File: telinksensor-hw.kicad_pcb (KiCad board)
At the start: 2 copper layers, 69 parts, among them Q1 2N7002, U1 TLSR8258

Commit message: Outline done
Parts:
- added AE1: Antenna, RF_Antenna:Johanson_2450AT18x100, F.Cu at (156.0, 46.4)
- added H1: MountingHole, MountingHole:MountingHole_3.2mm_M3_Pad_Via, F.Cu at (149.5, 104.4)
- added H2: MountingHole, MountingHole:MountingHole_3.2mm_M3_Pad_Via, F.Cu at (182.3, 104.5)
- added J1: ANT, Connector_Coaxial:U.FL_Molex_MCRF_73412-0110_Vertical, F.Cu at (150.1, 47.7)
- added J2: 3W RTD, TerminalBlock:TerminalBlock_bornier-3_P5.08mm, F.Cu at (176.1, 112.8)
- added J4: RTD 2W, TerminalBlock:TerminalBlock_bornier-2_P5.08mm, F.Cu at (160.8, 112.8)
- added J5: SOIC bite, soicbite:SOIC_clipProgSmall, F.Cu at (185.2, 73.4)
- added L1: 47u, Inductor_SMD:L_0805_2012Metric, F.Cu at (120.4, 46.5)
- added L2: 1n3, Inductor_SMD:L_0402_1005Metric, F.Cu at (126.5, 109.7)
- added L3: 3n3, Inductor_SMD:L_0402_1005Metric, F.Cu at (114.5, 73.8)
- added SW1: SW_Push, Button_Switch_SMD:SW_SPST_EVQPE1, F.Cu at (180.9, 112.9)
- added U2: SHT40, sensirion:SHT40, F.Cu at (186.2, 115.6)
- added U3: BMP390, bosh:BMP390, F.Cu at (145.7, 115.3)
- added Y1: 24MHz, Crystal:Crystal_SMD_3225-4Pin_3.2x2.5mm, F.Cu at (109.9, 74.8)
- C19, C20, C21, C22, C23, C24: footprint Capacitor_SMD:C_0603_1608Metric -> Capacitor_SMD:C_0402_1005Metric
- R8: footprint Resistor_SMD:R_0603_1608Metric -> Resistor_SMD:R_0402_1005Metric
- TP1, TP10, TP2, TP3, TP4, TP5, TP6, TP7, TP8, TP9: footprint TestPoint:TestPoint_Pad_1.5x1.5mm -> TestPoint:TestPoint_Pad_D1.0mm
- moved R2 63.8 mm to (166.5, 131.2)
- moved R8 60.6 mm to (150.1, 51.8), turned to 90 degrees
- moved R14 58.8 mm to (85.2, 42.7)
- moved R18 58.8 mm to (57.0, 58.9)
- moved R19 58.8 mm to (57.0, 63.9)
- moved R9 58.8 mm to (85.2, 45.2)
- moved TP1 58.8 mm to (80.3, 61.9)
- moved TP5 58.8 mm to (90.1, 53.3)
- moved C11 58.8 mm to (70.8, 52.8)
- moved C12 58.8 mm to (65.0, 64.8)
- moved C16 58.8 mm to (73.0, 57.8)
- moved C18 58.8 mm to (70.8, 50.3)
- moved C19 58.8 mm to (82.8, 50.3)
- moved C2 58.8 mm to (73.1, 45.2)
- moved C20 58.8 mm to (73.0, 60.3)
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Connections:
- R8 pad 1: Net-(AE1-Pad1) -> Net-(C20-Pad1)
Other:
- board outline added: 44 x 33.5 mm
- copper layers 2 -> 4

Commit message: Routing mostly done
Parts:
- removed C24: 1p, Capacitor_SMD:C_0402_1005Metric
- removed C29: 100n, Capacitor_SMD:C_0603_1608Metric
- AE1: value Antenna -> Antenna_Shield; footprint RF_Antenna:Johanson_2450AT18x100 -> RF_Antenna:Texas_SWRA117D_2.4GHz_Left
- C10, C12, C13, C14, C15, C16, C28, C3, C30, C5, C6, C7, C8, C9: footprint Capacitor_SMD:C_0603_1608Metric -> Capacitor_SMD:C_0402_1005Metric
- C17: value 100n -> 1p; footprint Capacitor_SMD:C_0603_1608Metric -> Capacitor_SMD:C_0402_1005Metric
- C18: value 1u -> 100p; footprint Capacitor_SMD:C_0603_1608Metric -> Capacitor_SMD:C_0402_1005Metric
- C20: value 2p7 -> 0p5
- C21: value 220p -> 2p7
- C22: value 2p -> 220p
- C23: value 0p5 -> 2p
- moved C30 139.2 mm to (186.2, 113.3), turned to 180 degrees
- moved D3 121.4 mm to (171.1, 102.1), turned to 180 degrees
- moved D2 121.0 mm to (167.1, 102.1)
- moved R5 118.9 mm to (176.9, 100.7), turned to 180 degrees
- moved C26 118.1 mm to (169.1, 106.4)
- moved TP4 115.6 mm to (185.9, 99.1), turned to 180 degrees
- moved C11 115.2 mm to (176.9, 97.7), turned to 180 degrees
- moved Q1 115.2 mm to (163.1, 106.7), turned to -90 degrees
- moved R17 114.3 mm to (174.3, 103.9), turned to 90 degrees
- moved C18 113.2 mm to (176.2, 91.5), turned to 90 degrees
- moved C25 112.9 mm to (167.5, 104.7)
- moved R18 112.9 mm to (159.4, 106.3)
- moved R19 111.5 mm to (159.4, 107.9)
- moved D4 111.1 mm to (156.0, 106.7), turned to 90 degrees
- moved U1 111.0 mm to (157.0, 96.5), turned to -90 degrees
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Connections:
- AE1 pad 2: (no net) -> GND
- C17 pad 1: VDD -> Net-(AE1-Pad1)
- C18 pad 1: VDD -> Net-(L3-Pad2)
- C18 pad 2: GND -> Net-(AE1-Pad1)
- C20 pad 1: Net-(C20-Pad1) -> Net-(L3-Pad2)
- C21 pad 1: Net-(C20-Pad1) -> Net-(C21-Pad1)
- C21 pad 2: Net-(C21-Pad2) -> GND
- C22 pad 1: Net-(C21-Pad2) -> Net-(C21-Pad1)
- C22 pad 2: GND -> Net-(C22-Pad2)
- C23 pad 1: Net-(AE1-Pad1) -> Net-(C22-Pad2)
- L2 pad 2: Net-(C20-Pad1) -> Net-(C21-Pad1)
- L3 pad 1: Net-(C21-Pad2) -> Net-(C22-Pad2)
- L3 pad 2: Net-(AE1-Pad1) -> Net-(L3-Pad2)
- R8 pad 1: Net-(C20-Pad1) -> Net-(L3-Pad2)
- U1 pad 27: Net-(C20-Pad1) -> Net-(C21-Pad1)
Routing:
- net /GND_RTD: track 0.00 -> 29.8 mm
- net /PGA-: track 0.00 -> 21.3 mm
- net /SENSOR_PWR: track 0.00 -> 21.2 mm
- net /PGA+: track 0.00 -> 21.1 mm
- net /I2C_SDA: track 0.00 -> 18.5 mm, vias 0 -> 2
- net Net-(C1-Pad1): track 0.00 -> 16.5 mm
- net /I2C_SCL: track 0.00 -> 16.5 mm, vias 0 -> 2
- net VDD: track 0.00 -> 16.3 mm, vias 0 -> 4
- net GND: track 0.00 -> 16.2 mm, vias 0 -> 88
- net /ADC3: track 0.00 -> 16.1 mm
- net Net-(J2-Pad3): track 0.00 -> 15.8 mm, vias 0 -> 1
- net +1V2: track 0.00 -> 15.8 mm, vias 0 -> 6
- net Net-(R13-Pad2): track 0.00 -> 14.9 mm
- net /SWM: track 0.00 -> 14.4 mm, vias 0 -> 1
- net Net-(L3-Pad2): track 0.00 -> 11.7 mm
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- added copper zone on B.Cu, net GND
- added copper zone on F.Cu, net GND
- added copper zone on In1.Cu, net GND
- added copper zone on In2.Cu, net VDD

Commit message: Routing almost done
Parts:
- D1, J2, J4, SW1: moved to B.Cu
- moved J2 10.2 mm to (165.9, 112.8), turned to 0 degrees
- moved J4 5.08 mm to (155.8, 112.8), turned to 0 degrees
- moved R3 3.30 mm to (150.9, 110.6), turned to 0 degrees
- moved D1 1.10 mm to (150.9, 112.8), turned to 180 degrees
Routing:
- net Net-(J2-Pad1): track 6.60 -> 14.7 mm
- net /GND_RTD: track 29.8 -> 22.9 mm
- net Net-(J4-Pad1): track 6.73 -> 10.4 mm
- net /BTN: track 4.79 -> 5.02 mm, vias 0 -> 1
- net Net-(D1-Pad1): track 2.22 -> 2.38 mm, vias 0 -> 1

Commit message: Routing done
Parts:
- removed J1: ANT, Connector_Coaxial:U.FL_Molex_MCRF_73412-0110_Vertical
- removed R8: 0R, Resistor_SMD:R_0402_1005Metric
- removed TP1: PGA+, TestPoint:TestPoint_Pad_D1.0mm
- removed TP3: PGA-, TestPoint:TestPoint_Pad_D1.0mm
- added BT1: CR2032-BS-6-1, Battery:BatteryHolder_Keystone_1060_1x2032, B.Cu at (165.9, 97.4)
- added TP11: MM8130-2600, murrata:MM8130-2600, F.Cu at (171.4, 97.2)
- moved TP4 41.3 mm to (145.4, 107.1)
- moved TP7 33.8 mm to (146.1, 99.1), turned to 0 degrees
- moved R5 31.4 mm to (146.4, 93.4), turned to 0 degrees
- moved R4 30.8 mm to (146.4, 94.9), turned to 180 degrees
- moved TP5 30.6 mm to (153.7, 110.1)
- moved C11 30.5 mm to (146.4, 96.4), turned to 0 degrees
- moved C4 10.8 mm to (155.2, 89.6), turned to 0 degrees
- moved R1 8.93 mm to (155.2, 88.1), turned to 180 degrees
- moved TP2 8.06 mm to (152.6, 91.4), turned to 180 degrees
- moved TP10 3.98 mm to (158.7, 87.5)
- moved TP9 0.60 mm to (164.7, 94.7)
- moved L1 0.10 mm to (152.4, 94.4)
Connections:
- C18 pad 1: Net-(L3-Pad2) -> Net-(C18-Pad1)
- C20 pad 1: Net-(L3-Pad2) -> Net-(C20-Pad1)
- J2 pad 1: Net-(J2-Pad1) -> Net-(R10-Pad2)
- J2 pad 3: Net-(J2-Pad3) -> Net-(R13-Pad1)
- L3 pad 2: Net-(L3-Pad2) -> Net-(C20-Pad1)
- R10 pad 2: Net-(J2-Pad3) -> Net-(R10-Pad2)
- R13 pad 1: Net-(J2-Pad1) -> Net-(R13-Pad1)
- R15 pad 2: Net-(J2-Pad1) -> Net-(R13-Pad1)
- R17 pad 1: Net-(J2-Pad3) -> Net-(R10-Pad2)
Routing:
- net /SENSOR_PWR: track 21.2 -> 94.0 mm, vias 0 -> 4
- net /I2C_SCL: track 16.5 -> 83.3 mm, vias 2 -> 4
- net /I2C_SDA: track 18.5 -> 75.7 mm, vias 2 -> 4
- net +1V2: track 15.8 -> 68.0 mm
- net /LED: track 1.49 -> 40.4 mm, vias 0 -> 3
- net /BTN: track 5.02 -> 42.0 mm, vias 1 -> 2
- net /~{RST}: track 1.71 -> 37.9 mm, vias 0 -> 2
- net /GND_RTD: track 22.9 -> 44.3 mm
- net /ADC1: track 4.14 -> 22.3 mm, vias 0 -> 2
- net Net-(J2-Pad3): track 15.8 -> 0.00 mm, vias 1 -> 0
- net /RTD_ON: track 2.17 -> 17.5 mm, vias 0 -> 2
- net Net-(J2-Pad1): track 14.7 -> 0.00 mm
- net Net-(R10-Pad2): track 0.00 -> 13.7 mm, vias 0 -> 1
- net /ADC2: track 0.87 -> 13.8 mm, vias 1 -> 2
- net Net-(L3-Pad2): track 11.7 -> 0.00 mm
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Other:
- board text added: "JLCJLCJLCJLC"
- board text added: "RTD"
- board text added: "TSENSOR V1.0 18.11. 2022"
- board text added: "Vojtěch Vosáhlo"

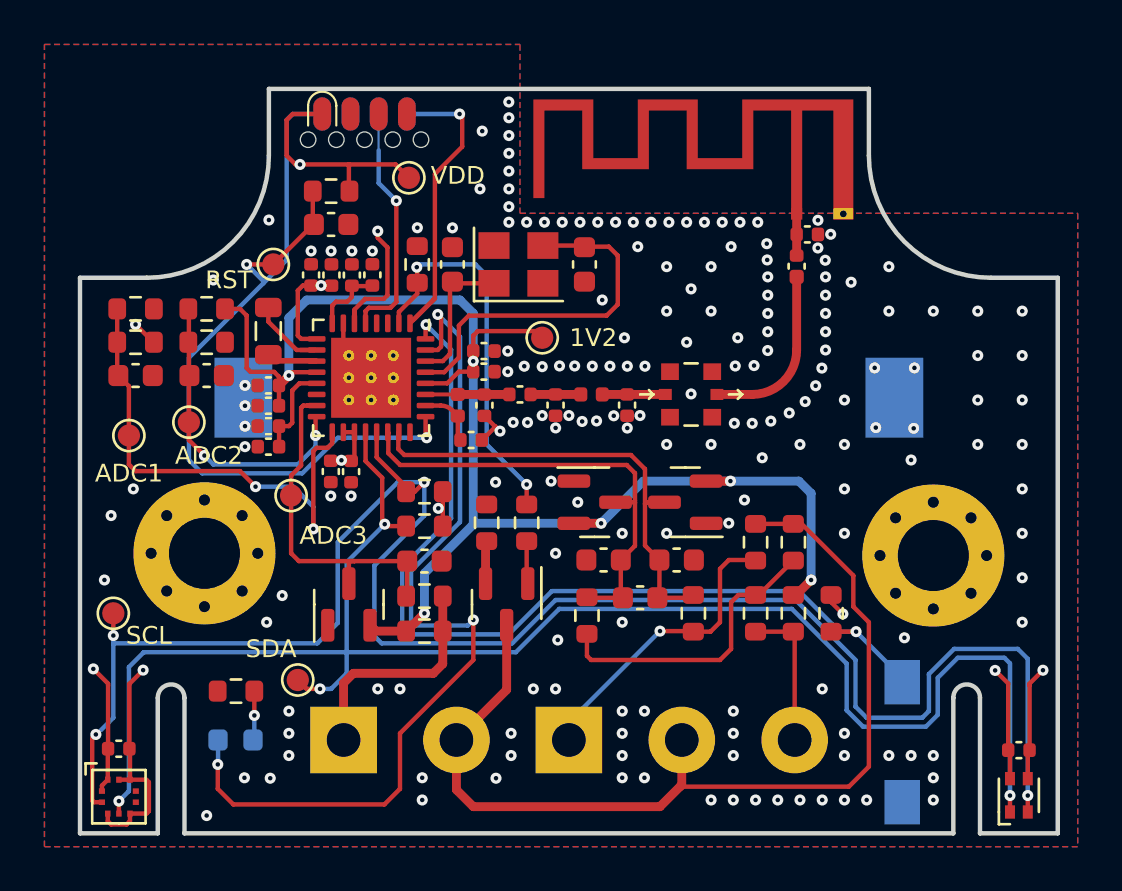
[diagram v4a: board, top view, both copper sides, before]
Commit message: Added teardrops
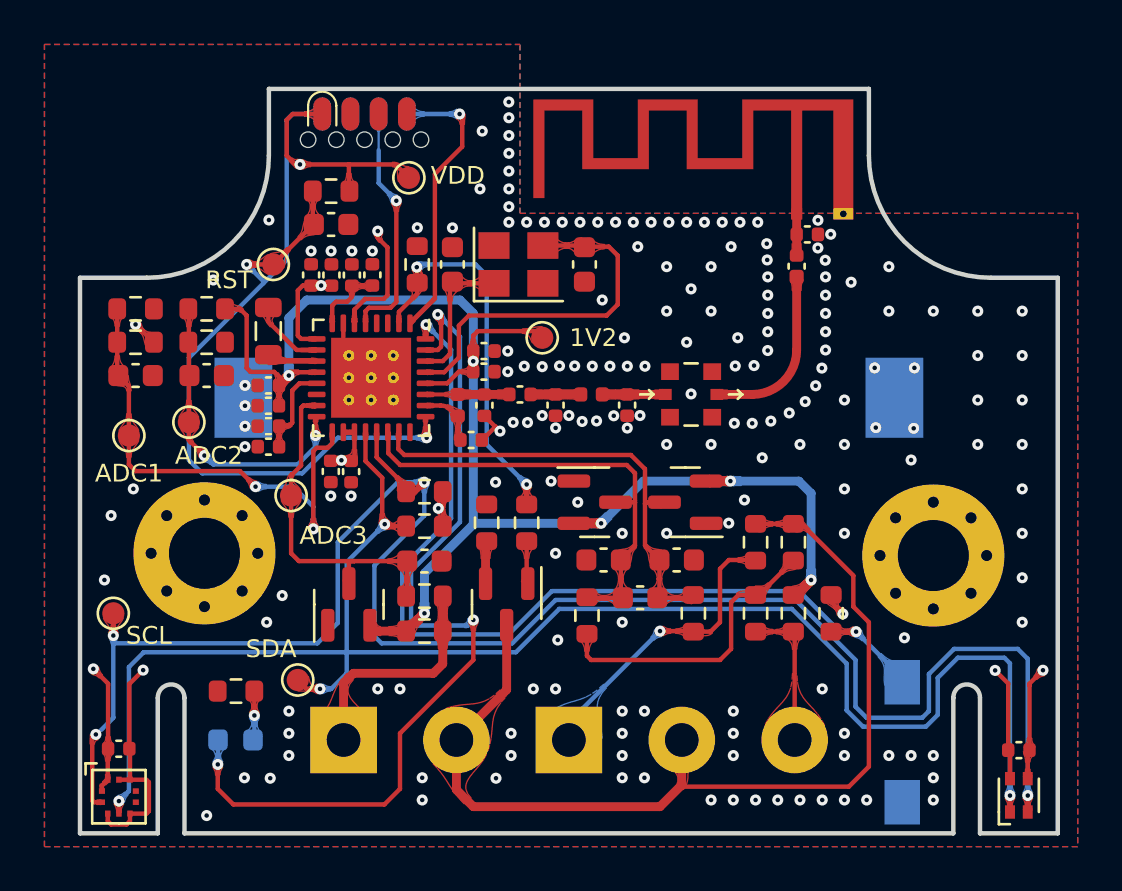
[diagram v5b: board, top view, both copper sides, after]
